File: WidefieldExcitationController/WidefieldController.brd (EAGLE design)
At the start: 108 x 25.4 mm, 29 parts, among them J1 5-1634503-1, J2 5-1634503-1, J3 5-1634503-1, J4 5-1634503-1

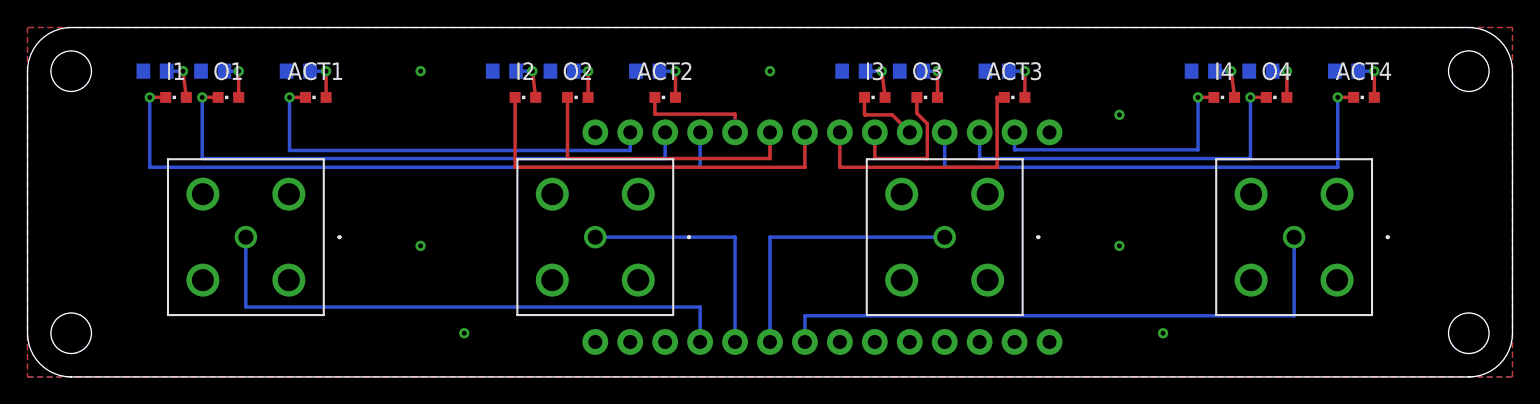
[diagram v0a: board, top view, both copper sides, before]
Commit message: Updated WidefieldController board to be smaller
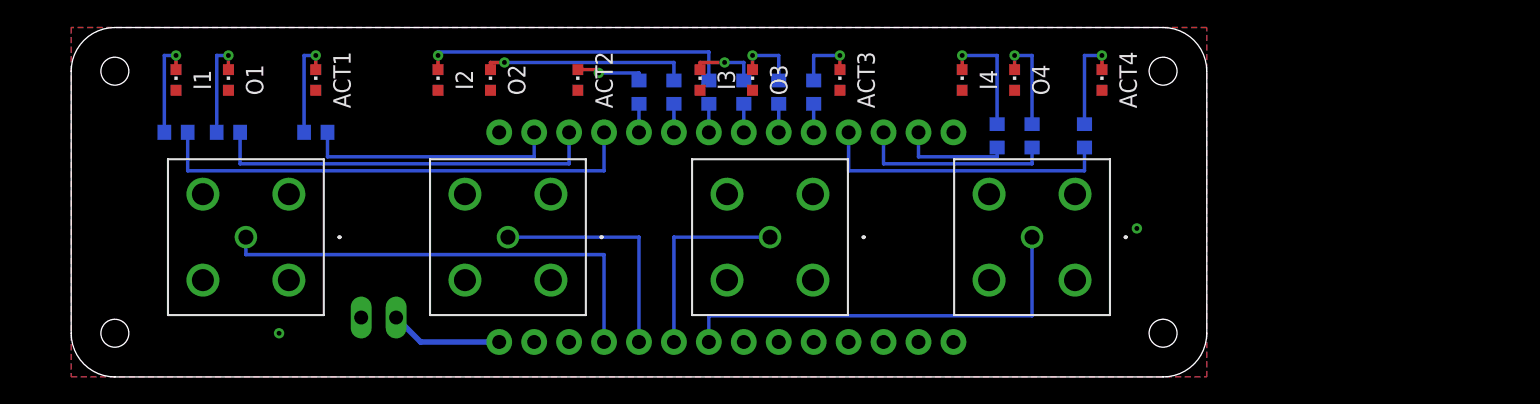
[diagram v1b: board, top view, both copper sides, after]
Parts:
- added VIN: (no value), pinhead:1X02
- moved R12 19.6 mm to (73.7, 17.5), turned to 90 degrees
- moved ACT4 19.1 mm to (74.9, 21.6), turned to 0 degrees
- moved I4 19.1 mm to (64.8, 21.6), turned to 0 degrees
- moved O4 19.1 mm to (68.6, 21.6), turned to 0 degrees
- moved J4 19.1 mm to (69.8, 10.2)
- moved R11 17.3 mm to (69.8, 17.5), turned to 90 degrees
- moved R10 15.7 mm to (67.3, 17.5), turned to 90 degrees
- moved R4 14.9 mm to (46.4, 20.7), turned to 90 degrees
- moved R9 13.4 mm to (54.0, 20.7), turned to 90 degrees
- moved I3 12.8 mm to (45.7, 21.6), turned to 0 degrees
- moved ACT3 12.8 mm to (55.9, 21.6), turned to 0 degrees
- moved O3 12.8 mm to (49.5, 21.6), turned to 0 degrees
- moved J3 12.7 mm to (50.8, 10.2)
- moved R8 9.77 mm to (51.4, 20.7), turned to 90 degrees
- moved R5 8.27 mm to (43.8, 20.7), turned to 90 degrees
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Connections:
- removed net VIN: IFN.VIN
- new net N$13: ACT1.C, R3.2
- net GND: now also ACT1.A, ACT2.A, ACT3.A, ACT4.A, I1.A, I2.A, I3.A, I4.A, O1.A, O2.A, O3.A, O4.A, VIN.1; no longer R1.2, R10.2, R11.2, R12.2, R2.2, R3.2, R4.2, R5.2, R6.2, R7.2, R8.2, R9.2
- net LED1A: now also R1.1; no longer I1.C
- net LED1B: now also R2.1; no longer O1.C
- net LED1C: now also R3.1; no longer ACT1.C
- net LED2A: now also R4.1; no longer I2.C
- net LED2B: now also R5.1; no longer O2.C
- net LED2C: now also R6.1; no longer ACT2.C
- net LED3A: now also IFN.6, R7.1; no longer I3.C, IFN.8
- net LED3B: now also R8.1; no longer O3.C
- net LED3C: now also IFN.8, R9.1; no longer ACT3.C, IFN.6
- net LED4A: now also R10.1; no longer I4.C
- net LED4B: now also R11.1; no longer O4.C
- net LED4C: now also R12.1; no longer ACT4.C
- net N$1: now also I2.C, R4.2; no longer I1.A, R1.1
- net N$10: now also I3.C, R7.2; no longer I4.A, R10.1
- net N$11: now also I1.C, R1.2; no longer O4.A, R11.1
- net N$12: now also O1.C, R2.2; no longer ACT4.A, R12.1
- net N$2: now also O2.C, R5.2; no longer O1.A, R2.1
- net N$3: now also ACT2.C, R6.2; no longer ACT1.A, R3.1
- net N$4: now also I4.C, R10.2; no longer I2.A, R4.1
- net N$5: now also O4.C, R11.2; no longer O2.A, R5.1
- net N$6: now also ACT4.C, R12.2; no longer ACT2.A, R6.1
- net N$7: now also IFN.VIN, VIN.2; no longer I3.A, R7.1
- net N$8: now also ACT3.C, R9.2; no longer O3.A, R8.1
- net N$9: now also O3.C, R8.2; no longer ACT3.A, R9.1
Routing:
- net LED2A: track 28.7 -> 2.07 mm
- net N$1: track 3.10 -> 23.0 mm
- net LED2B: track 21.1 -> 2.07 mm
- net LED3C: track 19.6 -> 2.07 mm
- net LED4C: track 37.4 -> 21.6 mm, vias 1 -> 0
- net LED1A: track 48.8 -> 35.9 mm, vias 1 -> 0
- net LED4B: track 27.2 -> 14.3 mm, vias 1 -> 0
- net LED1B: track 41.2 -> 28.5 mm, vias 1 -> 0
- net LED1C: track 31.1 -> 18.6 mm, vias 1 -> 0
- net N$2: track 2.95 -> 15.2 mm
- net IO4: track 43.2 -> 31.1 mm
- net LED4A: track 19.6 -> 8.17 mm, vias 1 -> 0
- net LED3B: track 10.5 -> 2.07 mm
- net N$13: track 0.00 -> 7.47 mm, vias 0 -> 1
- net IO1: track 40.6 -> 33.7 mm
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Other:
- board size 108 x 25.4 mm -> 82.5 x 25.4 mm
